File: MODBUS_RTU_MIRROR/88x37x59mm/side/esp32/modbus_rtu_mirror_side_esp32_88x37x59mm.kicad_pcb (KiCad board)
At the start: 2 copper layers, 52 x 40 mm, 41 parts, among them J1 Conn_01x04_Male, J2 Conn_01x04_Male, J3 Conn_01x06_Male, J4 Conn_01x07_Male, J5 Conn_01x07_Male, SW1 SW_Push, U1 ESP32-WROOM-32, U2 TXS0108EPW, U3 AMS1117-3.3, U4 DS3231MZ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

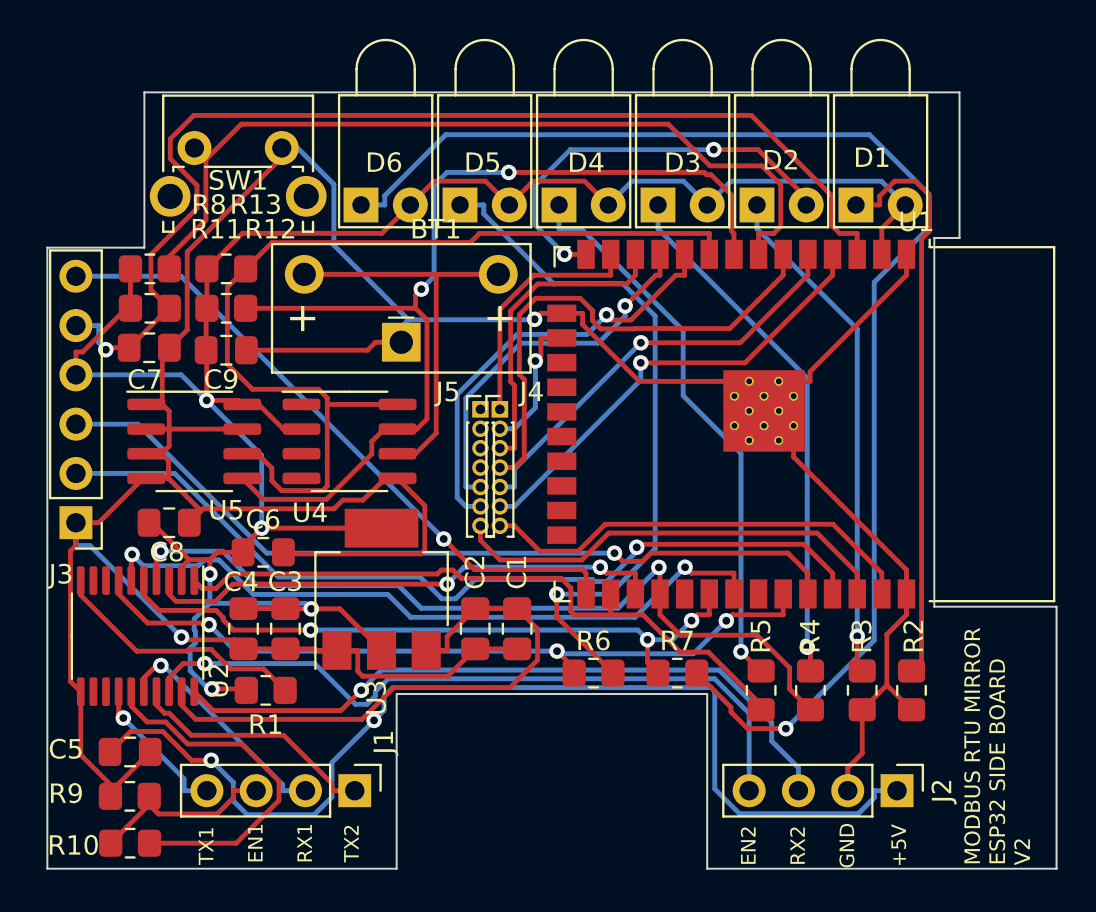
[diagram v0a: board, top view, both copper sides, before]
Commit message: added mech support pins for expansion board
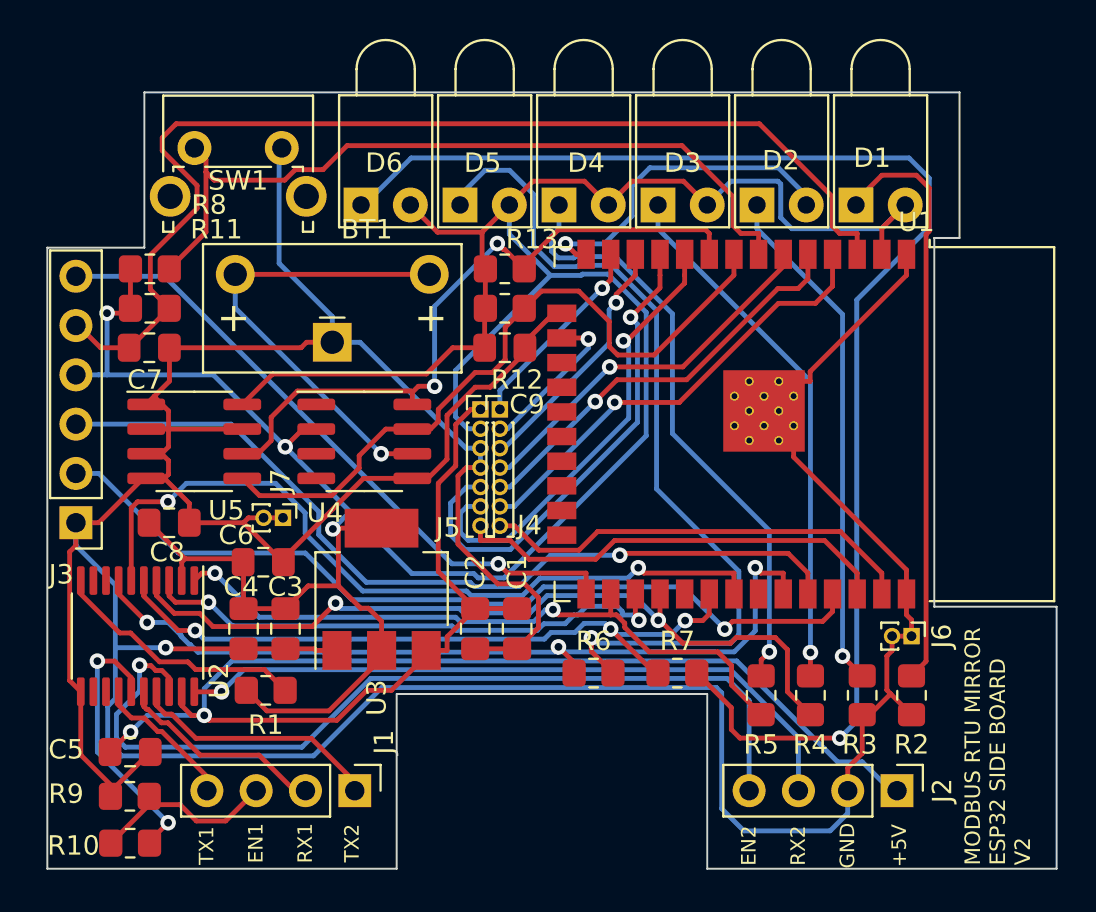
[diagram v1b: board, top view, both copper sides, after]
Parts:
- added J6: Conn_01x02_Male, Connector_PinHeader_1.00mm:PinHeader_1x02_P1.00mm_Vertical, F.Cu at (144.5, 128.0)
- added J7: Conn_01x02_Male, Connector_PinHeader_1.00mm:PinHeader_1x02_P1.00mm_Vertical, F.Cu at (112.1, 121.9)
- moved C9 14.4 mm to (123.6, 113.2)
- moved R12 14.3 mm to (123.6, 111.1)
- moved R13 14.3 mm to (123.6, 109.1)
- moved BT1 3.56 mm to (114.7, 112.9)
- moved U4 0.76 mm to (116.3, 118.0)
- moved C6 0.51 mm to (111.1, 124.2)
- moved R2 0.25 mm to (144.5, 131.1)
- moved R3 0.25 mm to (142.0, 131.1)
- moved R4 0.25 mm to (139.3, 131.1)
- moved R5 0.25 mm to (136.8, 131.1)
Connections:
- J5 pad 1: unconnected-(J5-Pad1) -> +5V
- J5 pad 2: unconnected-(J5-Pad2) -> +3.3V
- J5 pad 3: unconnected-(J5-Pad3) -> GND
- J5 pad 4: unconnected-(J5-Pad4) -> GND
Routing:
- net +3.3V: track 116.4 -> 162.0 mm, vias 5 -> 3
- net GND: track 192.2 -> 236.3 mm, vias 2 -> 1
- net /I2C0_SDA: track 52.7 -> 36.7 mm, vias 2 -> 0
- net /I2C0_SCL: track 50.7 -> 35.0 mm, vias 0 -> 2
- net Net-(J2-Pad4): track 37.2 -> 46.1 mm
- net Net-(D5-Pad1): track 36.0 -> 44.4 mm
- net /ESP_IO34: track 26.1 -> 19.5 mm, vias 0 -> 1
- net /ESP_IO26: track 19.3 -> 25.6 mm
- net Net-(R10-Pad2): track 18.5 -> 14.1 mm, vias 0 -> 2
- net +5V: track 84.0 -> 79.6 mm
- net /STP_LED: track 21.4 -> 17.3 mm, vias 2 -> 1
- net Net-(U1-Pad31): track 36.2 -> 40.1 mm
- net /TX1_LED: track 39.6 -> 43.1 mm
- net +BATT: track 20.6 -> 24.0 mm, vias 0 -> 1
- net /ESP_IO27: track 16.2 -> 13.0 mm, vias 0 -> 1
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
